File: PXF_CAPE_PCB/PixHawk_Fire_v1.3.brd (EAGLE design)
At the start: 86.4 x 54.6 mm, 242 parts, among them J305 DF13-3P-1.25V, J306 DF13-4P-1.25V, J307 DF13-4P-1.25V, J308 DF13-4P-1.25V, J309 DF13-5P-1.25V, J310 DF13-4P-1.25V, J314 DF13-4P-1.25V, J701 JST-ZH-3, J801 DF13C-6P-1.25V, M3_MOUNT901 MOUNT-HOLE3.1MM, M3_MOUNT902 MOUNT-HOLE3.1MM, M3_MOUNT903 MOUNT-HOLE3.1MM, M3_MOUNT904 MOUNT-HOLE3.1MM, Q501 MMBT3906LT1SMD, U1 EEPROM-I2CSMD, U102 FM25V01, U2 EEPROM-I2CSMD, U201 TXS0108QFN20, U202 TXS0108QFN20, U301 MAX3051, U302 TXS0108QFN20, U303 PCA9306, U401 MS5611-01BA, U402 MS5611-01BA, U403 MPU-6000, U405 MPU-9250, U406 LSM9DS0LSM9DS0, U407 BMP280_PRELIM, U501 BQ24315, U502 MIC5332, U503 BQ24315, U601 TCA62724FMG, U602 LT3469, U603 LRTB GFTG-T7AW-1+V7A7-29+R5T9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, U701 TXS0108QFN20, U702 TXS0108QFN20, U703 74LVC2G240, U704 BBB_3X14_RA, U801 BQ24313, U802 MIC5332, X801 4 pin head

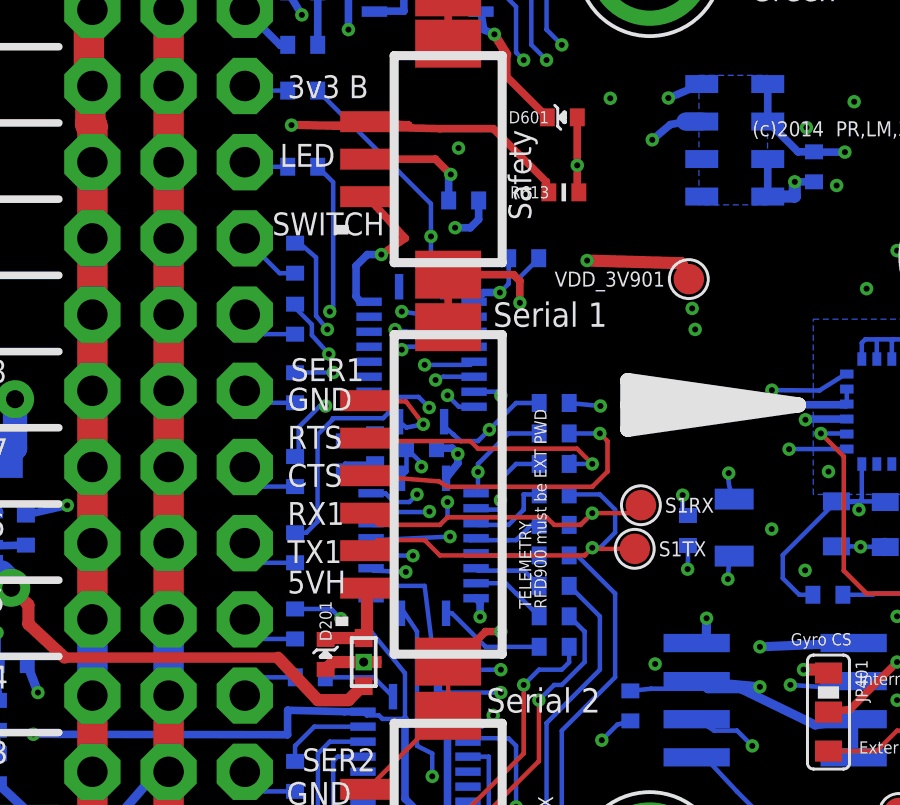
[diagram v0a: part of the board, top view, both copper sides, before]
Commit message: ISSUE#3 v2: Removal of the Voltage Trns. U702
Removal of U702, R718 and C703. Retracing of this area. Notice there is
a airwire in point 3880,929.5. I have tried to remove it with little
success.
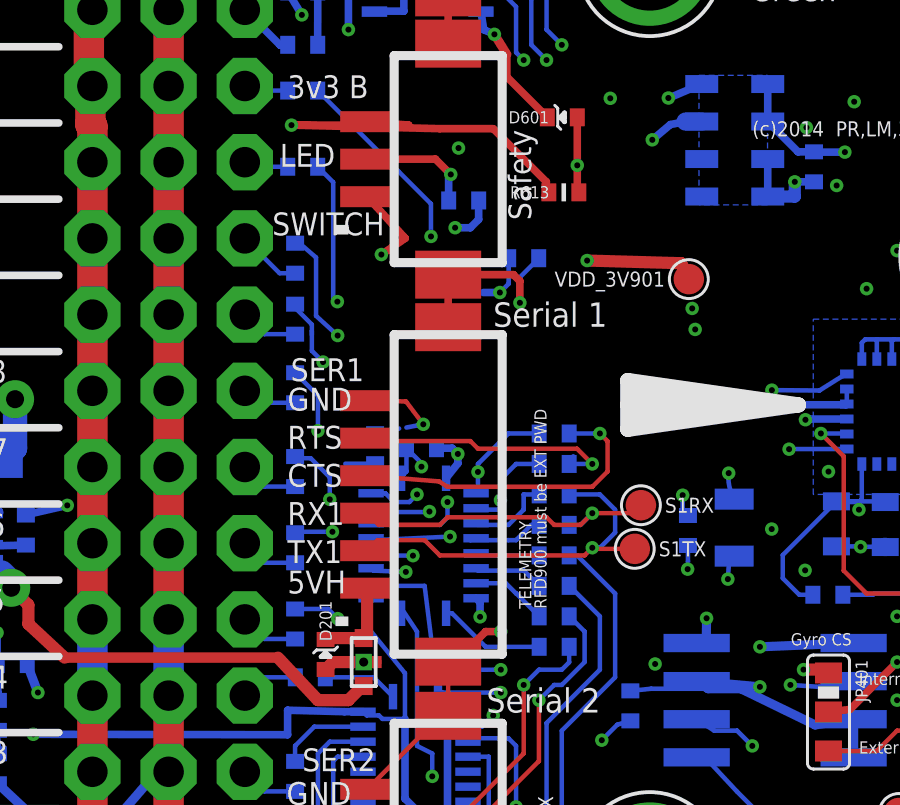
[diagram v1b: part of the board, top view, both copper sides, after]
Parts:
- removed C703: 0u1, pixhawk2:0402-CAP
- removed R718: 10K, pixhawk2:0402-RES
- removed U702: TXS0108QFN20, pixhawk2:QFN20-RGY
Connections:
- net BBB-VDD_3V3: no longer C703.P$1, R718.P$2, U702.10, U702.19, U702.2
- net CH_10: no longer U702.4
- net CH_11: no longer U702.3
- net CH_12: no longer U702.1
- net CH_5: no longer U702.9
- net CH_6: no longer U702.8
- net CH_7: no longer U702.7
- net CH_8: no longer U702.6
- net CH_9: no longer U702.5
- net GND: no longer C703.P$2, R718.P$1, U702.11
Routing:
- net CH_6: track 38.6 -> 22.8 mm, vias 2 -> 1
- net CH_5: track 33.1 -> 21.1 mm, vias 2 -> 1
- net CH_7: track 34.2 -> 26.0 mm, vias 2 -> 1
- net BBB-VDD_3V3: track 168.6 -> 161.3 mm, vias 20 -> 19
- net CH_8: track 31.4 -> 25.4 mm, vias 2 -> 1
- net CH_9: track 36.5 -> 31.6 mm, vias 2 -> 1
- net CH_11: track 43.2 -> 38.4 mm, vias 2 -> 1
- net CH_10: track 36.2 -> 31.9 mm, vias 2 -> 1
- net GND: track 460.9 -> 458.7 mm, vias 68 -> 67
- net CH_12: track 47.6 -> 45.7 mm
